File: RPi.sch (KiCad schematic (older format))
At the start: 1 part, among them X3 Raspberry_Pi_2_3

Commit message: Schematic is done except RF.
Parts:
- removed X3: Raspberry_Pi_2_3, Pin_Headers:Pin_Header_Straight_2x20, symbol Raspberry_Pi_2_3
- added R8: 0, Resistors_SMD:R_0402, symbol R
- added X3: RaspberryPiConnector, Pin_Headers:Pin_Header_Straight_2x20_Pitch2.54mm, symbol RaspberryPiConnector
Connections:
- net labels added: +3V3, CFG_MCLK, CFG_MISO, CFG_MOSI, RPI_A0, RPI_A1, RPI_A2, RPI_A3, RPI_A4, RPI_A5, RPI_A[0..5], RPI_D0, RPI_D1, RPI_D10, RPI_D11, RPI_D12, RPI_D13, RPI_D14, RPI_D15, RPI_D16, RPI_D17, RPI_D2, RPI_D3, RPI_D4, RPI_D5, RPI_D6, RPI_D7, RPI_D8, RPI_D9, RPI_D[0..31], RPI_GPIO1, ~CFG_CS, ~CFG_HOLD
- net labels removed: FT_D0, FT_D1, FT_D2, FT_D[0..2]
- wire segments 9 -> 39
- no-connect marks 2 -> 0

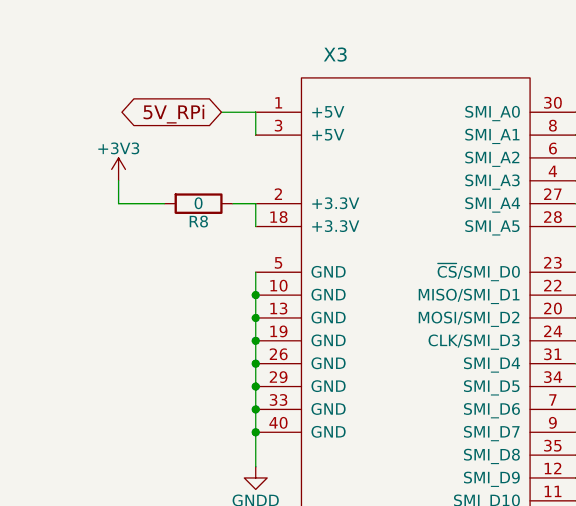
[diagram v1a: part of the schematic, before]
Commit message: Placed most components for FTDI. Begin tracing FT601
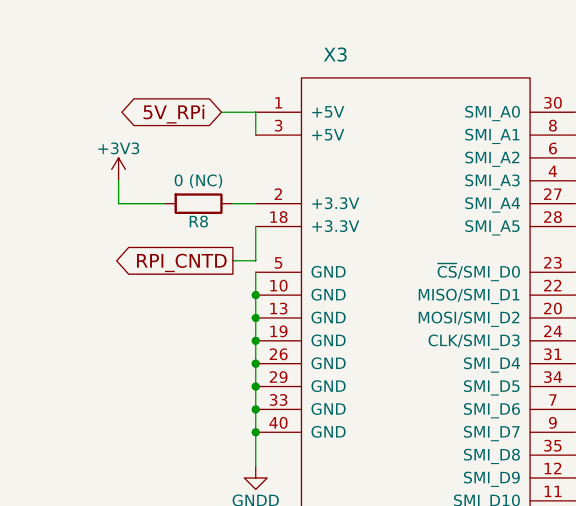
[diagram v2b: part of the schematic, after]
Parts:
- R8: value 0 -> 0 (NC); footprint Resistors_SMD:R_0402 -> Resistors_SMD:R_0603
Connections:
- net at R8.1, X3.2 (+3.3V): no longer X3.18 (+3.3V)
- new net RPI_CNTD: X3.18 (+3.3V)
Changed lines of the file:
@@
 EESchema Schematic File Version 2
-LIBS:sdr-rescue
 LIBS:power
 LIBS:device
@@
 LIBS:sdr
 LIBS:usb-type-c
-LIBS:sdr-cache
 EELAYER 25 0
 EELAYER END
@@
 P 1150 1350
 F 0 "R8" V 1230 1350 50  0000 C CNN
-F 1 "0" V 1150 1350 50  0000 C CNN
-F 2 "Resistors_SMD:R_0402" V 1080 1350 50  0001 C CNN
+F 1 "0 (NC)" V 1050 1350 50  0000 C CNN
+F 2 "Resistors_SMD:R_0603" V 1080 1350 50  0001 C CNN
 F 3 "" H 1150 1350 50  0000 C CNN
 	1    1150 1350
@@
 $EndComp
 $Comp
-L +3V3 #PWR035
+L +3V3 #PWR036
 U 1 1 58A418F6
 P 800 1250
-F 0 "#PWR035" H 800 1100 50  0001 C CNN
+F 0 "#PWR036" H 800 1100 50  0001 C CNN
 F 1 "+3V3" H 800 1390 50  0000 C CNN
 F 2 "" H 800 1250 50  0000 C CNN
@@
 $EndComp
 $Comp
-L GNDD #PWR036
+L GNDD #PWR037
 U 1 1 58A80C0C
 P 1400 2500
-F 0 "#PWR036" H 1400 2250 50  0001 C CNN
+F 0 "#PWR037" H 1400 2250 50  0001 C CNN
 F 1 "GNDD" H 1400 2350 50  0000 C CNN
 F 2 "" H 1400 2500 50  0000 C CNN
@@
 Wire Wire Line
 	800  1350 800  1250
-Wire Wire Line
-	1400 1350 1400 1450
 Wire Wire Line
 	1400 950  1400 1050
@@
 Wire Wire Line
 	3600 1250 3300 1250
+Text GLabel 1300 1600 0    60   Output ~ 0
+RPI_CNTD
+Wire Wire Line
+	1300 1600 1400 1600
+Wire Wire Line
+	1400 1600 1400 1450
 $EndSCHEMATC

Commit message: Right before Sitch power retracing
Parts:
- added U4: ECP5, sdr-foots:ECP5_381, symbol ECP5
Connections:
- new net FT_D0: U4.A17 (PT62A)
- new net FT_D1: U4.B17 (PT60A)
- new net FT_D2: U4.A18 (PT65A)
- new net FT_D3: U4.B18 (PT62B)
- new net FT_D4: U4.B19 (PT65B)
- new net FT_D5: U4.C17 (PT60B)
- no-connect marks 0 -> 4
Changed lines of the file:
@@
 LIBS:sdr
 LIBS:usb-type-c
+LIBS:sdr-cache
 EELAYER 25 0
 EELAYER END
@@
 $EndComp
 $Comp
-L +3V3 #PWR036
+L +3V3 #PWR037
 U 1 1 58A418F6
 P 800 1250
-F 0 "#PWR036" H 800 1100 50  0001 C CNN
+F 0 "#PWR037" H 800 1100 50  0001 C CNN
 F 1 "+3V3" H 800 1390 50  0000 C CNN
 F 2 "" H 800 1250 50  0000 C CNN
@@
 $EndComp
 $Comp
-L GNDD #PWR037
+L GNDD #PWR038
 U 1 1 58A80C0C
 P 1400 2500
-F 0 "#PWR037" H 1400 2250 50  0001 C CNN
+F 0 "#PWR038" H 1400 2250 50  0001 C CNN
 F 1 "GNDD" H 1400 2350 50  0000 C CNN
 F 2 "" H 1400 2500 50  0000 C CNN
@@
 	3150 3350 3250 3250
 Text GLabel 3600 1550 2    60   BiDi ~ 0
-RPI_D[0..31]
+RPI_D[0..17]
 Text Label 3250 3400 0    60   ~ 0
-RPI_D[0..31]
+RPI_D[0..17]
 Entry Wire Line
 	3250 1650 3350 1550
@@
 Wire Wire Line
 	1400 1600 1400 1450
+Wire Bus Line
+	7200 2550 7200 700
+Wire Bus Line
+	7200 700  5000 700
+Wire Bus Line
+	5000 700  5000 2550
+$Comp
+L ECP5 U4
+U 8 1 58B6A811
+P 5700 2500
+F 0 "U4" H 6100 2450 60  0000 C CNN
+F 1 "ECP5" H 5800 2450 60  0000 C CNN
+F 2 "sdr-foots:ECP5_381" H 4150 3050 60  0001 C CNN
+F 3 "" H 4150 3050 60  0001 C CNN
+	8    5700 2500
+	1    0    0    -1
+$EndComp
+Text GLabel 4600 2400 0    60   BiDi ~ 0
+FT_D[31..0]
+Text Label 5050 700  0    60   ~ 0
+FT_D[31..0]
+Entry Wire Line
+	4900 2400 5000 2500
+Wire Wire Line
+	4600 2400 4900 2400
+Text Label 5150 1900 0    60   ~ 0
+FT_D0
+Text Label 6800 2400 0    60   ~ 0
+FT_D1
+Text Label 5150 2400 0    60   ~ 0
+FT_D2
+Text Label 6800 1500 0    60   ~ 0
+FT_D3
+Text Label 5150 1300 0    60   ~ 0
+FT_D4
+Text Label 5150 2100 0    60   ~ 0
+FT_D5
+NoConn ~ 6700 1900
+NoConn ~ 6700 2100
+NoConn ~ 8700 2100
+$Comp
+L ECP5 U4
+U 9 1 58B6B1BD
+P 8900 2400
+F 0 "U4" H 9300 2350 60  0000 C CNN
+F 1 "ECP5" H 9000 2350 60  0000 C CNN
+F 2 "sdr-foots:ECP5_381" H 7350 2950 60  0001 C CNN
+F 3 "" H 7350 2950 60  0001 C CNN
+	9    8900 2400
+	1    0    0    -1
+$EndComp
+NoConn ~ 8700 1200
+Entry Wire Line
+	5000 2000 5100 2100
+Entry Wire Line
+	7100 1500 7200 1400
+Wire Wire Line
+	7100 1500 6700 1500
+Wire Wire Line
+	5500 2100 5100 2100
+Entry Wire Line
+	5000 1200 5100 1300
+Wire Wire Line
+	5100 1300 5500 1300
+Entry Wire Line
+	5000 1800 5100 1900
+Entry Wire Line
+	5000 2300 5100 2400
+Entry Wire Line
+	7100 2400 7200 2300
+Wire Wire Line
+	7100 2400 6700 2400
+Wire Wire Line
+	5100 1900 5500 1900
+Wire Wire Line
+	5500 2400 5100 2400
 $EndSCHEMATC

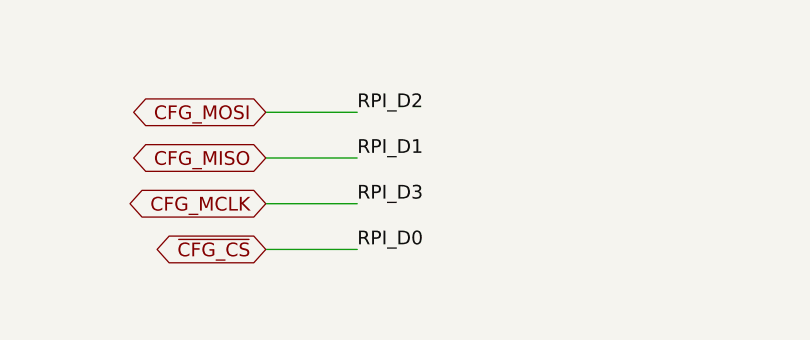
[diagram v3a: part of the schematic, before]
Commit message: Caps for FPGA are placed. Most of FPGA power is traced. Need to trace Rpi connector
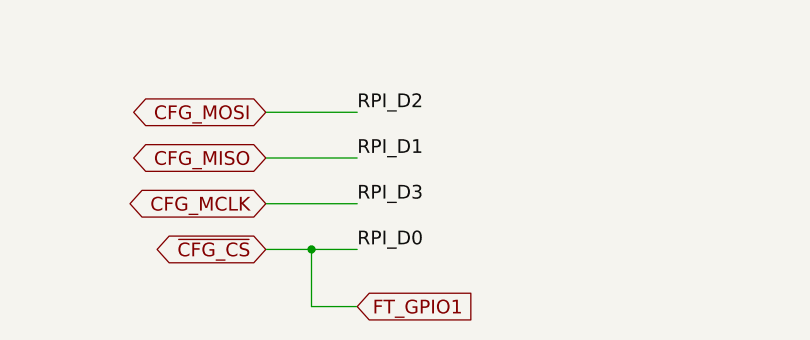
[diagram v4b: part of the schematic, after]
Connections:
- net ~CFG_CS renamed FT_GPIO1
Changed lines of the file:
@@
 $EndComp
 $Comp
-L +3V3 #PWR037
+L +3V3 #PWR038
 U 1 1 58A418F6
 P 800 1250
-F 0 "#PWR037" H 800 1100 50  0001 C CNN
+F 0 "#PWR038" H 800 1100 50  0001 C CNN
 F 1 "+3V3" H 800 1390 50  0000 C CNN
 F 2 "" H 800 1250 50  0000 C CNN
@@
 $EndComp
 $Comp
-L GNDD #PWR038
+L GNDD #PWR039
 U 1 1 58A80C0C
 P 1400 2500
-F 0 "#PWR038" H 1400 2250 50  0001 C CNN
+F 0 "#PWR039" H 1400 2250 50  0001 C CNN
 F 1 "GNDD" H 1400 2350 50  0000 C CNN
 F 2 "" H 1400 2500 50  0000 C CNN
@@
 Wire Wire Line
 	5500 2400 5100 2400
+Text GLabel 2000 4950 2    60   Input ~ 0
+FT_GPIO1
+Wire Wire Line
+	2000 4950 1800 4950
+Wire Wire Line
+	1800 4950 1800 4700
+Connection ~ 1800 4700
 $EndSCHEMATC

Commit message: All traced except Rpi and LMS
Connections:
- net ~RPI_WE: now reaches X3.25 (~WE)
- net ~RPI_OE: now reaches X3.32 (~OE)
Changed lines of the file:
@@
 	1800 4950 1800 4700
 Connection ~ 1800 4700
+Text Label 1000 3050 0    60   ~ 0
+~RPI_OE
+Text Label 1000 2950 0    60   ~ 0
+~RPI_WE
+Wire Wire Line
+	1400 2950 1000 2950
+Wire Wire Line
+	1000 3050 1400 3050
 $EndSCHEMATC

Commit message: RPI is almost finished
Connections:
- net RPI_A0: now also U4.A12 (PT40A)
- net RPI_A1: now also U4.A7 (PT18A)
- net RPI_A4: now also U4.B12 (PT35A)
- net RPI_D10: now also U4.A9 (PT24A)
- net RPI_D11: now also U4.B16 (PT56B)
- net RPI_D12: now also U4.A16 (PT56A)
- net RPI_D14: now also U4.A10 (PT27A)
- net RPI_D15: now also U4.B11 (PT29A)
- net RPI_D17: now also U4.A11 (PT27B)
- net RPI_D4: now also U4.C13 (PT42B)
- net RPI_D5: now also U4.B13 (PT42A)
- net RPI_D6: now also U4.B8 (PT15B)
- net RPI_D7: now also U4.A8 (PT18B)
- net RPI_D8: now also U4.A14 (PT47A)
- net RPI_D9: now also U4.B9 (PT22A)
- net RPI_GPIO1: now also U4.C10 (PT22B)
- net ~RPI_OE: now also U4.A13 (PT40B)
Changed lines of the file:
@@
 	1400 1600 1400 1450
 Wire Bus Line
-	7200 2550 7200 700
-Wire Bus Line
-	7200 700  5000 700
+	7200 700  7200 2550
 Wire Bus Line
 	5000 700  5000 2550
@@
 NoConn ~ 6700 1900
 NoConn ~ 6700 2100
-NoConn ~ 8700 2100
 $Comp
 L ECP5 U4
@@
 Text Label 1000 3050 0    60   ~ 0
 ~RPI_OE
-Text Label 1000 2950 0    60   ~ 0
-~RPI_WE
 Wire Wire Line
-	1400 2950 1000 2950
+	950  2950 1400 2950
 Wire Wire Line
 	1000 3050 1400 3050
+Text Label 5150 1700 0    60   ~ 0
+RPI_D12
+Text Label 5150 2300 0    60   ~ 0
+RPI_D11
+Text Label 6800 1000 0    60   ~ 0
+RPI_D8
+Text Label 6800 1300 0    60   ~ 0
+RPI_D5
+Text Label 8300 1400 0    60   ~ 0
+RPI_D6
+Text Label 8300 1300 0    60   ~ 0
+RPI_D7
+Text Label 7450 1650 0    60   ~ 0
+RPI_D8
+Text Label 10000 1800 0    60   ~ 0
+RPI_D9
+Text Label 6800 1200 0    60   ~ 0
+~RPI_OE
+Text Label 5150 1200 0    60   ~ 0
+RPI_D4
+Text Label 5150 1000 0    60   ~ 0
+RPI_A0
+Text Label 10000 2200 0    60   ~ 0
+RPI_A1
+Text Label 7500 2300 0    60   ~ 0
+RPI_A2
+Text Label 7500 2400 0    60   ~ 0
+RPI_A3
+Text Label 6800 900  0    60   ~ 0
+RPI_A4
+Text Label 7500 2600 0    60   ~ 0
+RPI_A5
+Text Label 7500 2700 0    60   ~ 0
+RPI_A6
+Text GLabel 950  2950 0    60   Output ~ 0
+~RPI_WE
+Text Label 10000 1900 0    60   ~ 0
+RPI_D17
+Entry Wire Line
+	7100 1600 7200 1500
+Wire Wire Line
+	6700 1600 7100 1600
+NoConn ~ 9900 1700
+Wire Wire Line
+	6700 1200 6800 1200
+Wire Wire Line
+	6800 900  6700 900
+Wire Wire Line
+	5500 1000 5150 1000
+Wire Wire Line
+	5150 1200 5500 1200
+Wire Wire Line
+	5500 1700 5150 1700
+Wire Wire Line
+	5150 2300 5500 2300
+Wire Wire Line
+	6700 1300 6800 1300
+Wire Wire Line
+	6800 1000 6700 1000
+Text Label 8300 2000 0    60   ~ 0
+RPI_D15
+Text Label 10000 2100 0    60   ~ 0
+RPI_D14
+Text Label 10000 1500 0    60   ~ 0
+RPI_GPIO1
+Text Label 10000 1400 0    60   ~ 0
+RPI_D10
+Wire Bus Line
+	5000 700  7200 700
+Wire Wire Line
+	10000 1400 9900 1400
+Wire Wire Line
+	9900 1500 10000 1500
+Wire Wire Line
+	10000 1800 9900 1800
+Wire Wire Line
+	9900 1900 10000 1900
+Wire Wire Line
+	10000 2100 9900 2100
+Wire Wire Line
+	8700 1300 8300 1300
+Wire Wire Line
+	8300 1400 8700 1400
+Wire Wire Line
+	8700 2000 8300 2000
+Wire Wire Line
+	10000 2200 9900 2200
 $EndSCHEMATC

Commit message: Everything is done except LMS and RF
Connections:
- net RPI_A0: now also U4.C13 (PT42B); no longer U4.A12 (PT40A)
- net RPI_A1: now also U4.B8 (PT15B); no longer U4.A7 (PT18A)
- net RPI_A2: now also U4.A7 (PT18A)
- net RPI_A3: now also U4.C6 (PT11A)
- net RPI_A4: now also U4.B15 (PT51A); no longer U4.B12 (PT35A)
- net RPI_D10: now also U4.B10 (PT24B); no longer U4.A9 (PT24A)
- net RPI_D14: now also U4.B11 (PT29A); no longer U4.A10 (PT27A)
- net RPI_D15: now also U4.A11 (PT27B); no longer U4.B11 (PT29A)
- net RPI_D16: now also U4.B12 (PT35A)
- net RPI_D17: now also U4.A12 (PT40A); no longer U4.A11 (PT27B)
- net RPI_D4: now also U4.A13 (PT40B); no longer U4.C13 (PT42B)
- net RPI_D6: now also U4.A8 (PT18B); no longer U4.B8 (PT15B)
- net RPI_D7: now also U4.B9 (PT22A); no longer U4.A8 (PT18B)
- net RPI_D9: now also U4.A9 (PT24A); no longer U4.B9 (PT22A)
- net RPI_GPIO1: now also U4.A10 (PT27A); no longer U4.C10 (PT22B)
- net ~RPI_OE: no longer U4.A13 (PT40B)
- net ~RPI_WE: now also U4.D11 (PT33A)
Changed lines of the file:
@@
 	1800 4950 1800 4700
 Connection ~ 1800 4700
-Text Label 1000 3050 0    60   ~ 0
-~RPI_OE
-Wire Wire Line
-	950  2950 1400 2950
 Wire Wire Line
 	1000 3050 1400 3050
@@
 Text Label 6800 1300 0    60   ~ 0
 RPI_D5
-Text Label 8300 1400 0    60   ~ 0
+Text Label 8300 1300 0    60   ~ 0
 RPI_D6
-Text Label 8300 1300 0    60   ~ 0
+Text Label 10000 1800 0    60   ~ 0
 RPI_D7
-Text Label 7450 1650 0    60   ~ 0
-RPI_D8
-Text Label 10000 1800 0    60   ~ 0
+Text Label 10000 1400 0    60   ~ 0
 RPI_D9
 Text Label 6800 1200 0    60   ~ 0
-~RPI_OE
+RPI_D4
 Text Label 5150 1200 0    60   ~ 0
-RPI_D4
+RPI_A0
+Text Label 8300 1400 0    60   ~ 0
+RPI_A1
+Text Label 10000 2200 0    60   ~ 0
+RPI_A2
+Text Label 8300 1900 0    60   ~ 0
+RPI_A3
 Text Label 5150 1000 0    60   ~ 0
-RPI_A0
-Text Label 10000 2200 0    60   ~ 0
-RPI_A1
-Text Label 7500 2300 0    60   ~ 0
-RPI_A2
-Text Label 7500 2400 0    60   ~ 0
-RPI_A3
-Text Label 6800 900  0    60   ~ 0
-RPI_A4
-Text Label 7500 2600 0    60   ~ 0
-RPI_A5
-Text Label 7500 2700 0    60   ~ 0
-RPI_A6
-Text GLabel 950  2950 0    60   Output ~ 0
-~RPI_WE
-Text Label 10000 1900 0    60   ~ 0
 RPI_D17
 Entry Wire Line
@@
 Wire Wire Line
 	6800 1000 6700 1000
+Text Label 10000 1900 0    60   ~ 0
+RPI_D15
 Text Label 8300 2000 0    60   ~ 0
-RPI_D15
+RPI_D14
 Text Label 10000 2100 0    60   ~ 0
-RPI_D14
-Text Label 10000 1500 0    60   ~ 0
 RPI_GPIO1
-Text Label 10000 1400 0    60   ~ 0
+Text Label 10000 1200 0    60   ~ 0
 RPI_D10
 Wire Bus Line
@@
 Wire Wire Line
 	10000 1400 9900 1400
-Wire Wire Line
-	9900 1500 10000 1500
 Wire Wire Line
 	10000 1800 9900 1800
@@
 Wire Wire Line
 	10000 2200 9900 2200
+Text Label 6800 900  0    60   ~ 0
+RPI_D16
+Wire Wire Line
+	10000 1200 9900 1200
+Text Label 5150 2000 0    60   ~ 0
+~RPI_WE
+Wire Wire Line
+	5150 2000 5500 2000
+Text Label 1000 2950 0    60   ~ 0
+~RPI_WE
+Wire Wire Line
+	1400 2950 1000 2950
+Text GLabel 1000 3050 0    60   Output ~ 0
+~RPI_OE
+Text Label 6800 1600 0    60   ~ 0
+RPI_A4
+Wire Wire Line
+	8700 1900 8300 1900
 $EndSCHEMATC
